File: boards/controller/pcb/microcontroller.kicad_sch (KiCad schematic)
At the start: 19 parts, among them SW3001 SW_Push, SW3002 SW_Push, U3001 STM32U575VITx, X3001 16MHz

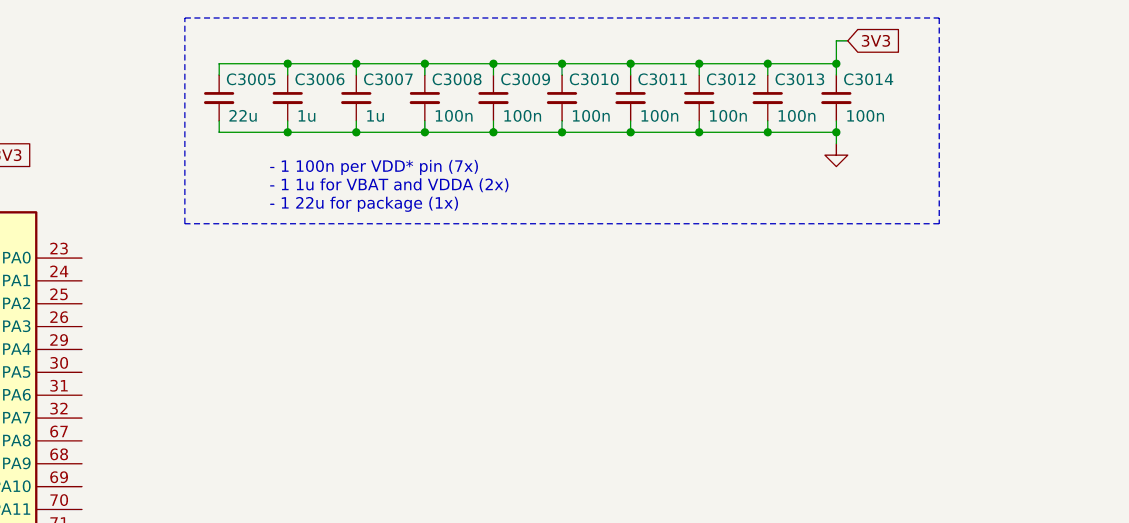
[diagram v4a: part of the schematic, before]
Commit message: controller: pcb: Update schematic
- Replace 22u caps with 10u since 22u are very expensive
- Add TCC and MPN fields

Signed-off-by: Nicholas Loehrke <nicholasnloehrke@gmail.com>
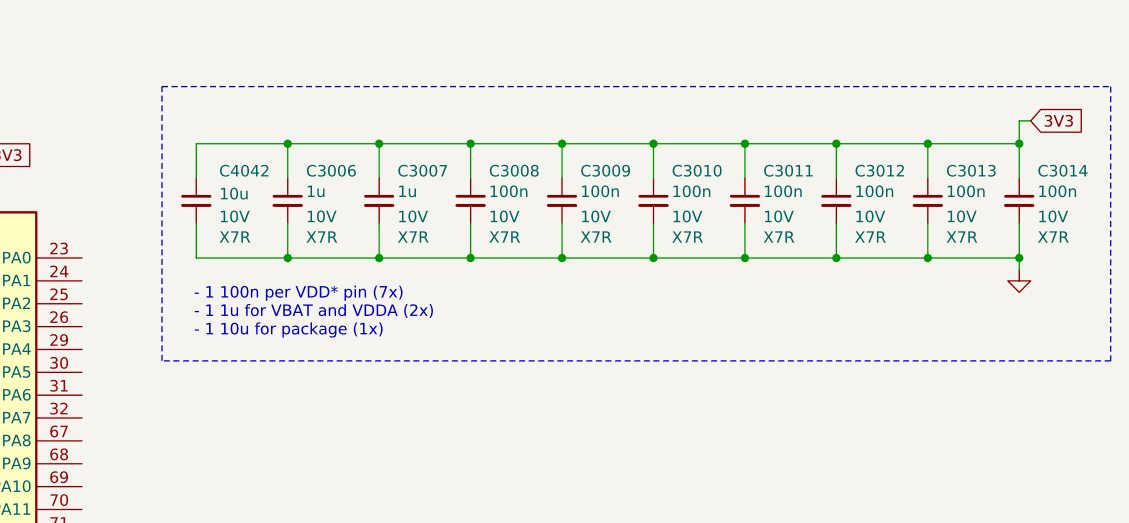
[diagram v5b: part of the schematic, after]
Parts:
- removed C3005: 22u, symbol Device:C_Small
- added C4042: 10u, symbol Device:C_Small
- C3006, C3007, C3008, C3009, C3010, C3011, C3012, C3013, C3014: TCC (none) -> X7R; Voltage (none) -> 10V
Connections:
- net 3V3: now also C4042.1
- net GND: now also C4042.2
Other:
- note added: "- 1 100n per VDD* pin (7x) - 1 1u for VBAT and VDDA (2x) - 1 10u for package (1x)"
- note removed: "- 1 100n per VDD* pin (7x) - 1 1u for VBAT and VDDA (2x) - 1 22u for package (1x)"
- moved on the sheet: C3006, C3008

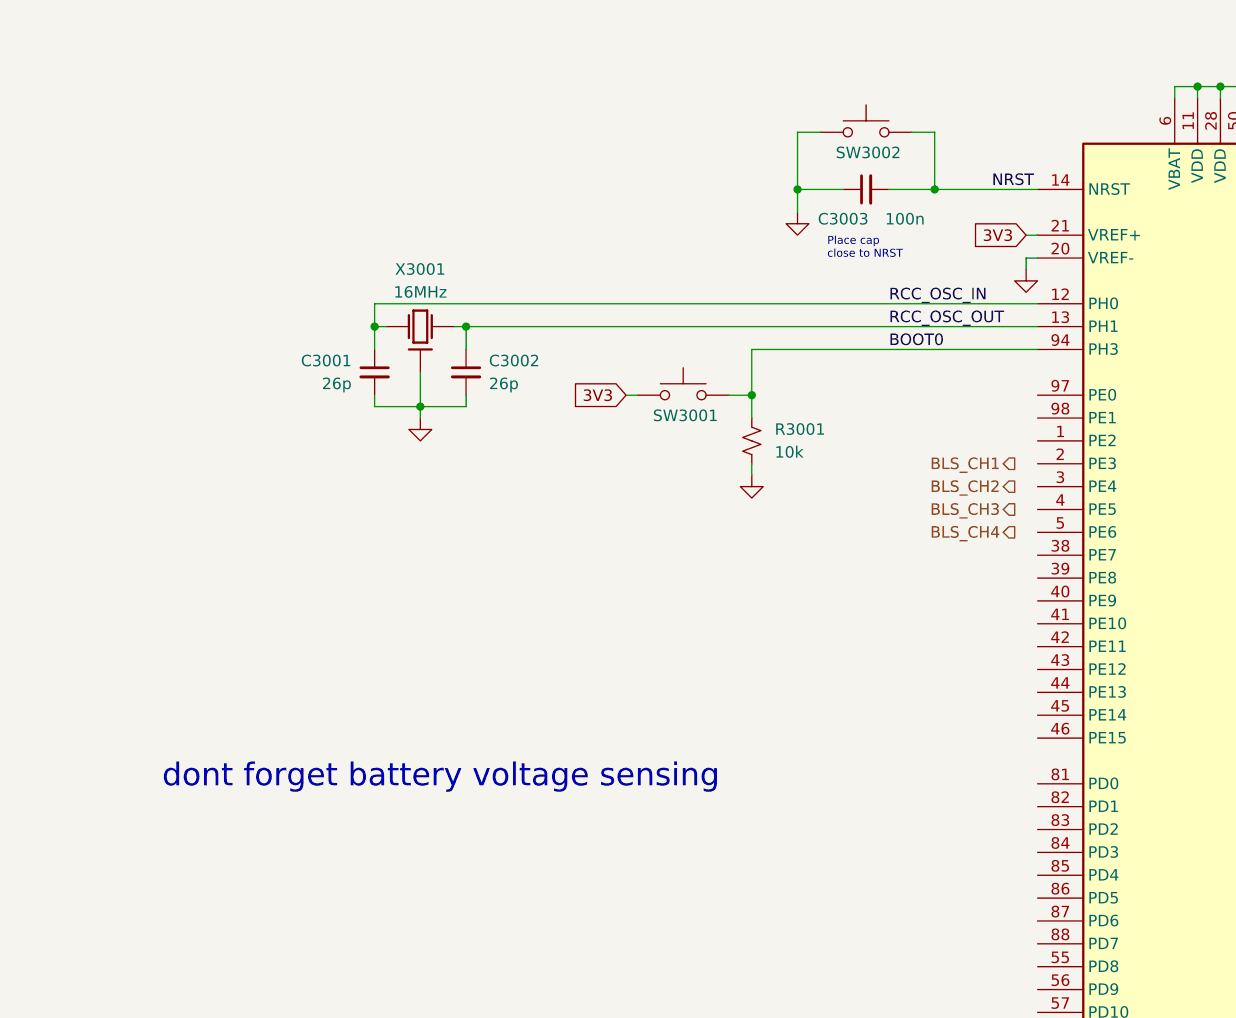
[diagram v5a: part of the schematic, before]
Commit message: controller: pcb: Update schematic
- Add TVS diodes on select MCU pins

Signed-off-by: Nicholas Loehrke <nicholasnloehrke@gmail.com>
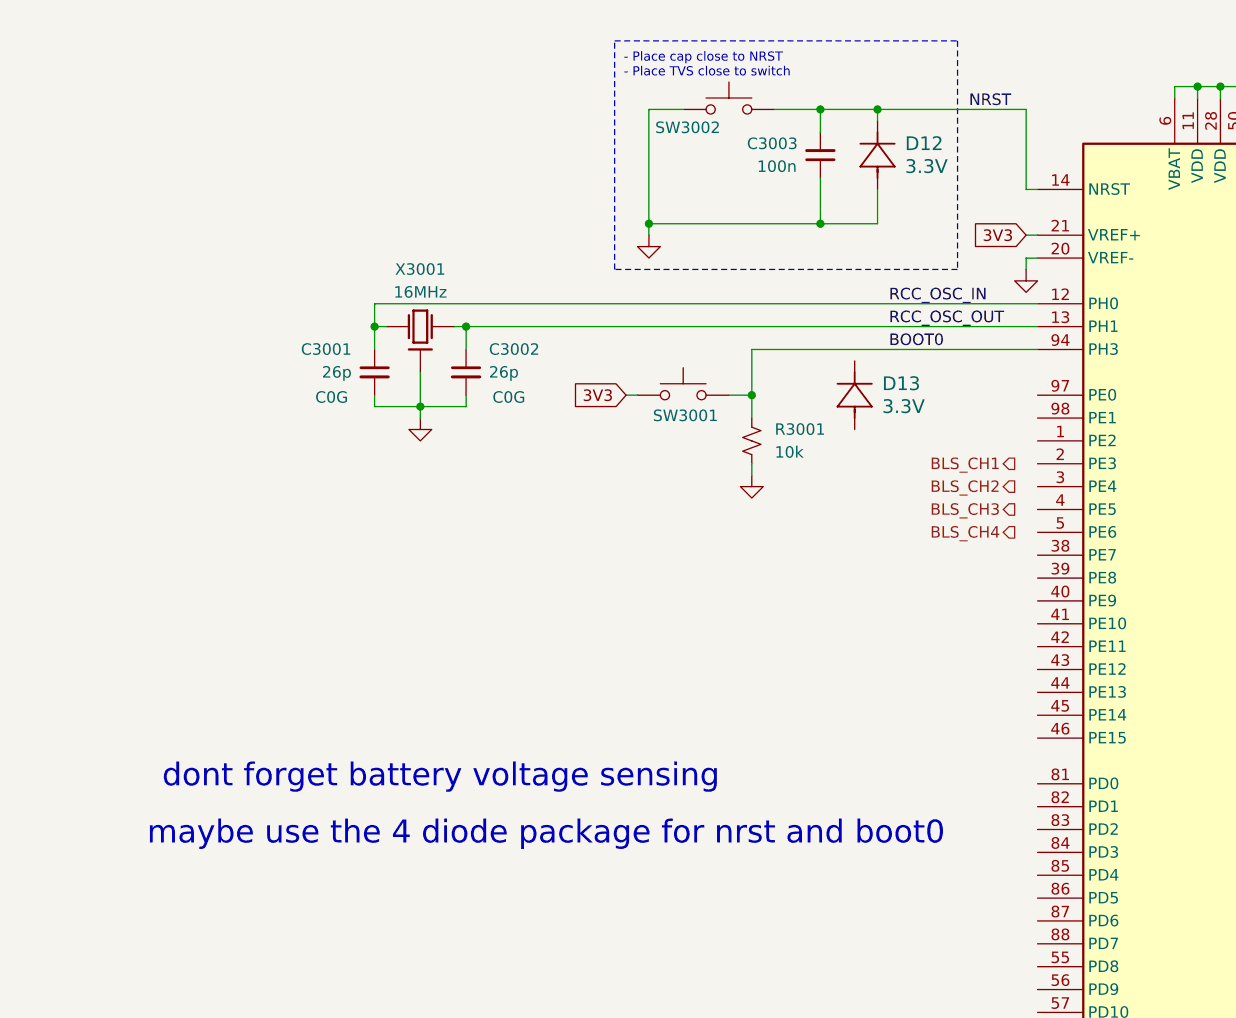
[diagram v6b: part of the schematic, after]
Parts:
- added D12, D13: 3.3V, CR_SOD-523_PNJ, symbol PJSD03TS-AU_R1_000A1:PJSD03TS-AU_R1_000A1
- C3001, C3002: TCC (none) -> C0G
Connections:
- net GND: now also D12.2
- net NRST: now also D12.1
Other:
- note added: "- Place cap close to NRST - Place TVS close to switch"
- note added: "maybe use the 4 diode package for nrst and boot0"
- note removed: "Place cap close to NRST"
- moved on the sheet: C3003, SW3002

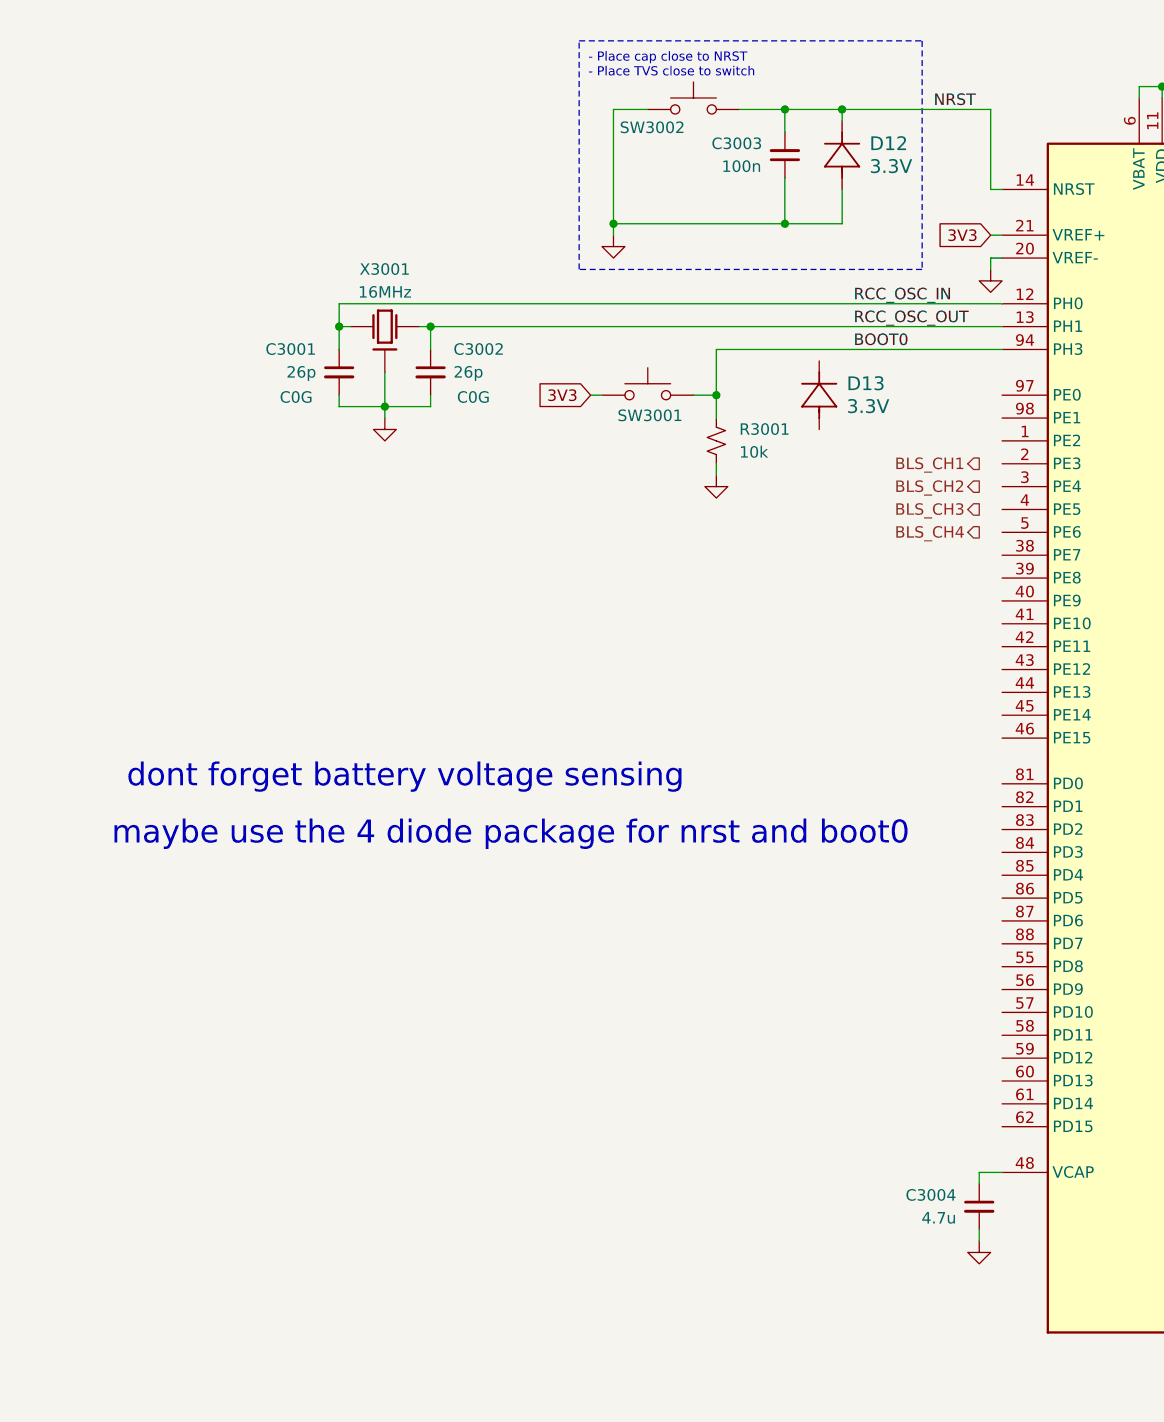
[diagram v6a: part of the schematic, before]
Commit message: controller: pcb: Update schematic
Signed-off-by: Nicholas Loehrke <nicholasnloehrke@gmail.com>
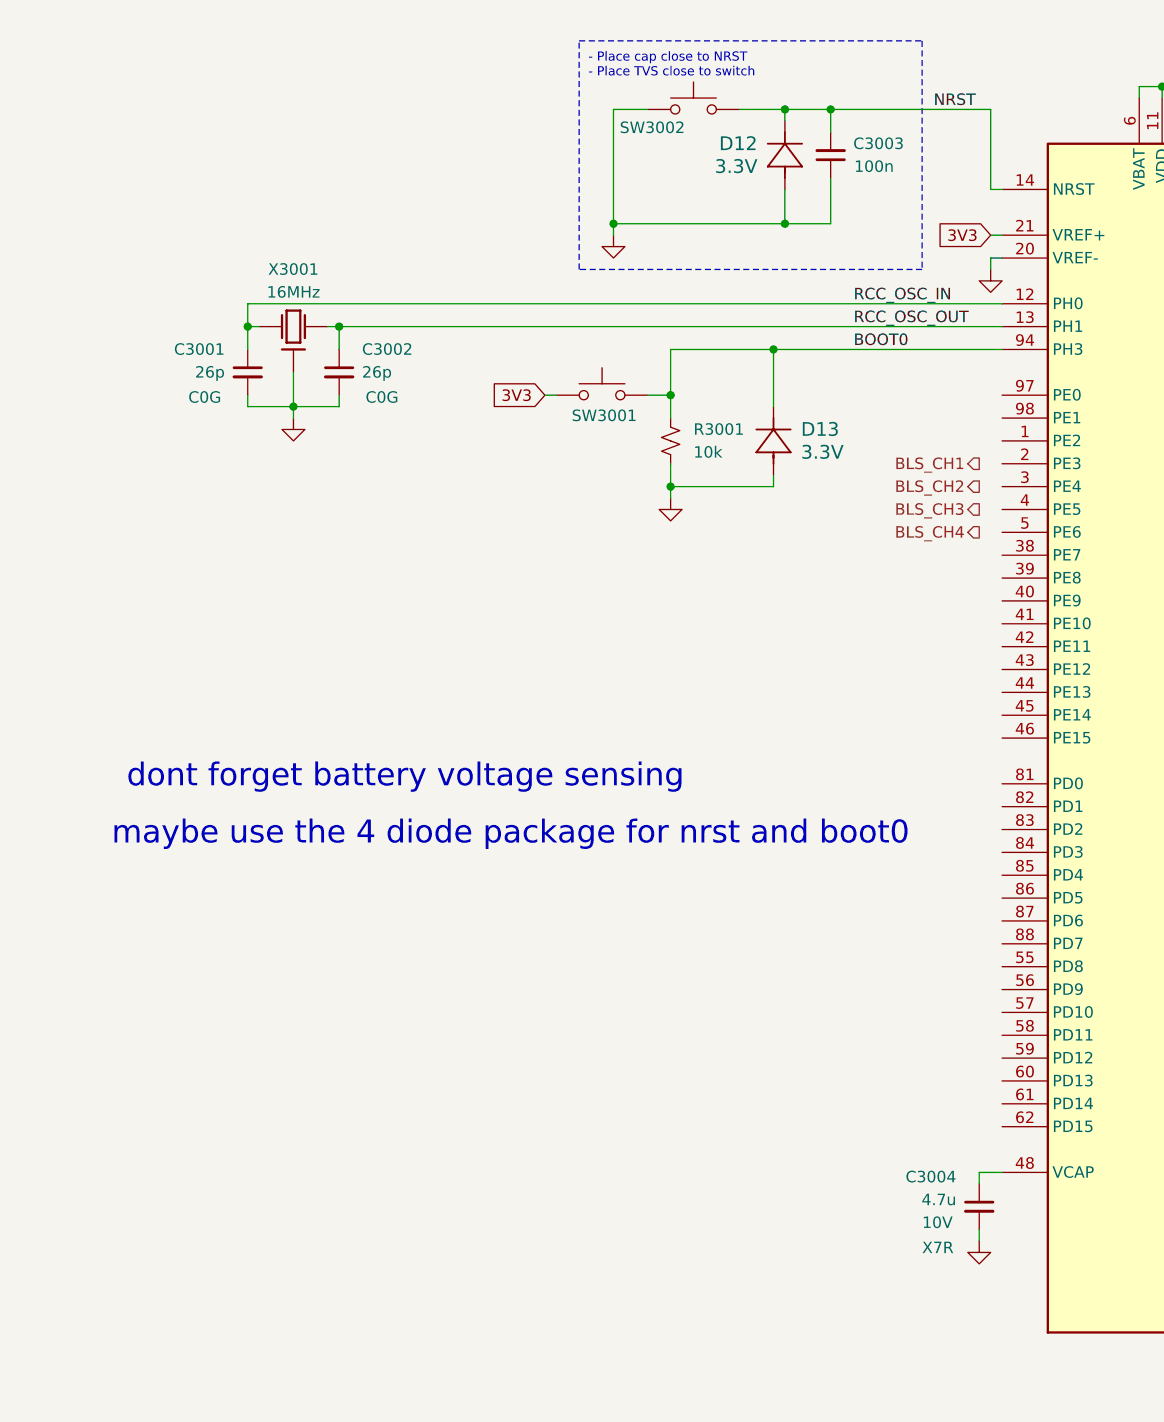
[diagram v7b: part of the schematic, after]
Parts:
- C3004: TCC (none) -> X7R; Voltage (none) -> 10V
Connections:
- net BOOT0: now also D13.1
- net GND: now also D13.2
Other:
- moved on the sheet: C3001, C3002, C3003, D12, D13, R3001, SW3001, X3001
